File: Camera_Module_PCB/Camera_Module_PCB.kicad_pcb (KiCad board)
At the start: 4 copper layers, 114 parts, among them J1 SS-52400-002, J2 Conn_01x02, J3 FFC2A32-24-T, SW1 SW_DIP_x01, SW2 SW_Push, SW3 SW_Push, U2 ESP32-S3R8, U4 MAX98357AETE_T, U5 AP3032KTR-G1, Y1 Q40,0-JXS10-8-10/10-FU-LF1

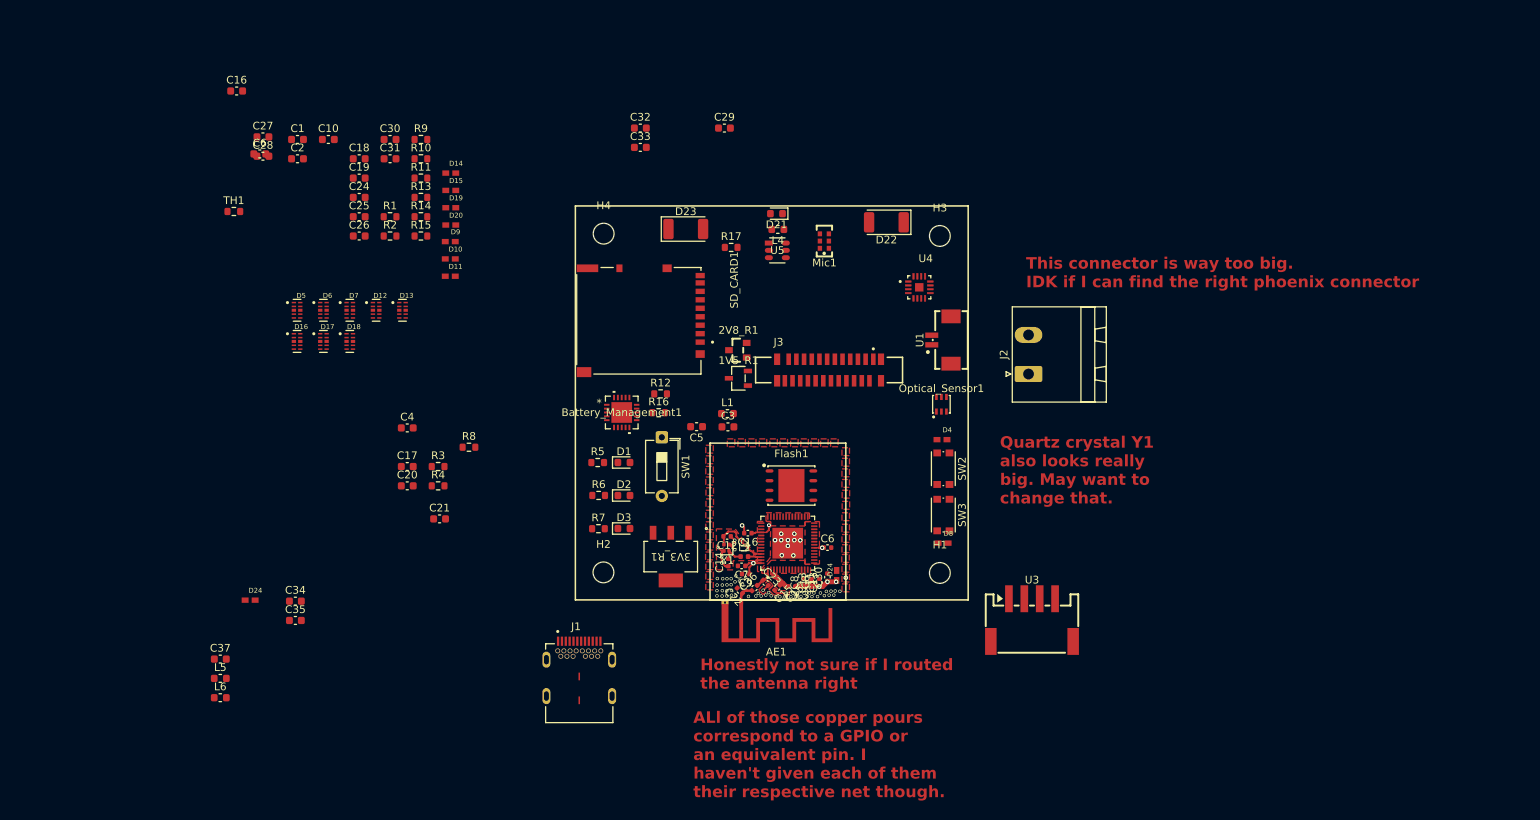
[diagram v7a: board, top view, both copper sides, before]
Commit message: Continued Routing of ESP32 chip and USB
Continued to create general layouts for the necessary ESP32 chip and power suuply
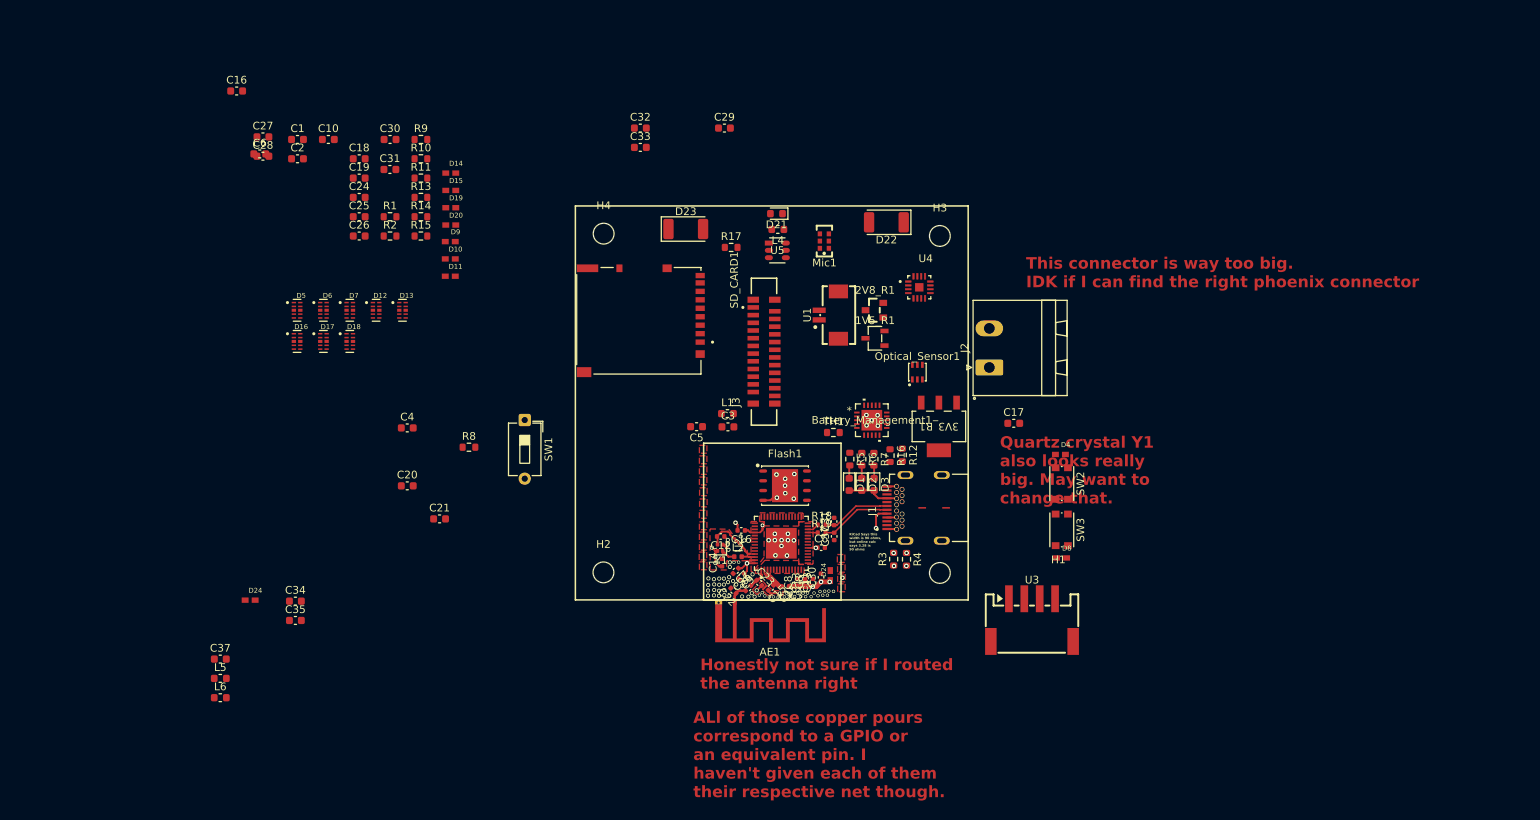
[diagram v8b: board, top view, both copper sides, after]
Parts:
- added C31: NC, Capacitor_SMD:C_0402_1005Metric, F.Cu at (135.2, 91.8)
- added C37: NC, Capacitor_SMD:C_0402_1005Metric, F.Cu at (135.2, 93.8)
- added R18: 22, Resistor_SMD:R_0402_1005Metric, F.Cu at (133.6, 92.2)
- added R19: 22, Resistor_SMD:R_0402_1005Metric, F.Cu at (133.6, 93.3)
- C22: value NG -> NC
- moved TH1 83.1 mm to (135.1, 80.2)
- moved C17 79.0 mm to (158.6, 79.0)
- moved R4 61.6 mm to (144.6, 96.7), turned to -90 degrees
- moved R3 60.4 mm to (143.0, 96.7), turned to 90 degrees
- moved J1 53.1 mm to (149.2, 90.0), turned to 90 degrees
- moved 3V3_R1 38.7 mm to (148.8, 79.5)
- moved R7 36.9 mm to (140.4, 83.7), turned to -90 degrees
- moved R6 34.5 mm to (138.8, 83.7), turned to -90 degrees
- moved D3 33.0 mm to (140.4, 87.0), turned to -90 degrees
- moved R5 32.8 mm to (137.3, 83.7), turned to -90 degrees
- moved Battery_Management1 32.5 mm to (140.1, 78.7)
- moved R12 32.4 mm to (144.1, 83.2), turned to -90 degrees
- moved D2 30.9 mm to (138.8, 87.0), turned to -90 degrees
- moved R16 30.6 mm to (142.5, 83.2), turned to -90 degrees
- moved D1 29.4 mm to (137.2, 87.0), turned to -90 degrees
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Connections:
- U2 pad 25: /USB_D- -> Net-(U2-GPIO19)
- U2 pad 26: /USB_D+ -> Net-(U2-GPIO20)
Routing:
- net /USB_D+: track 0.00 -> 9.24 mm
- net /USB_D-: track 0.00 -> 9.03 mm
- net /Power Supply/5V_USB: track 0.00 -> 8.16 mm
- net Net-(J1-CC2): track 0.00 -> 8.15 mm, vias 0 -> 1
- net Net-(J1-CC1): track 0.00 -> 7.28 mm, vias 0 -> 2
- net GND: track 10.2 -> 16.4 mm, vias 69 -> 93
- net Net-(D1-K): track 0.00 -> 1.75 mm
- net Net-(D3-K): track 0.00 -> 1.68 mm
- net Net-(D2-K): track 0.00 -> 1.68 mm
- net Net-(U2-GPIO20): track 0.00 -> 1.64 mm
- net Net-(U2-GPIO19): track 0.00 -> 1.30 mm
- net +3.3V: track 43.7 -> 44.2 mm
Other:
- board text added: "KiCad Says this width is 90 ohms, but online calc says 3.28 is 90 ohms"
